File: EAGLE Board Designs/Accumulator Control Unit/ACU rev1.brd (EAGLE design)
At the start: 186.7 x 135.7 mm, 187 parts, among them J1 CONNECTOR-CAN_MF_T_V_, J2 CONNECTOR-8_MF_T_V_, J3 CONNECTOR-8_MF_T_V_, J4 CONNECTOR-2_MF_T_V_, J5 CONNECTOR-12_MF_T_V_, Q1 TRANSISTOR_N_MOS__PMV15ENEA, Q2 TRANSISTOR_N_MOS__PMV15ENEA, T1 TRANSFORMER_HM2112ZNLT_AIRGAP, U10 OPAMP_1_CHANNEL_OPA991, U11 LOGICGATE_AND_DCK3, U12 OPAMP_1_CHANNEL_OPA991, U13 OPAMP_1_CHANNEL_OPA991, U14 OPAMP_1_CHANNEL_OPA991, U15 LOGICGATE_AND_DCK3, U18 OPAMP_1_CHANNEL_OPA991, U19 MAX7404, U2 ADG1423, U20 OPAMP_1_CHANNEL_OPA991, U22 OPAMP_1_CHANNEL_OPA991, U25 TCAN1051HQV-Q1, U26 MAX7404, U27 OPAMP_1_CHANNEL_OPA991, U28 MAX7404, U29 OPAMP_1_CHANNEL_OPA991, U3 LM555, U30 MAX7404, U4 OPAMP_1_CHANNEL_OPA991, U5 LTC6820, U6 ADM823, U7 OPAMP_1_CHANNEL_OPA991, U8 LOGICGATE_AND_DCK3, U9 OPAMP_1_CHANNEL_OPA991

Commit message: minor via changes
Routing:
- net GND: track 187.6 -> 189.1 mm
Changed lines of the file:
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@@
 <drawing>
 <settings>
-<setting alwaysvectorfont="yes"/>
+<setting alwaysvectorfont="no"/>
 <setting verticaltext="up"/>
 </settings>
@@
 <wire x1="29.90349375" y1="59.00191875" x2="29.91529375" y2="59.01371875" width="0.1524" layer="1"/>
 <via x="29.91529375" y="59.01371875" extent="1-16" drill="0.3048" diameter="0.55"/>
-<wire x1="28.42939375" y1="58.04851875" x2="28.42939375" y2="59.28041875" width="0.1524" layer="1"/>
-<wire x1="28.42939375" y1="59.28041875" x2="28.46749375" y2="59.31851875" width="0.1524" layer="1"/>
-<via x="28.46749375" y="59.31851875" extent="1-16" drill="0.3048" diameter="0.55"/>
+<wire x1="28.42939375" y1="58.04851875" x2="28.42939375" y2="58.69621875" width="0.1524" layer="1"/>
+<wire x1="29.66129375" y1="59.92811875" x2="29.99149375" y2="59.92811875" width="0.1524" layer="1"/>
+<wire x1="29.66129375" y1="59.92811875" x2="28.42939375" y2="58.69621875" width="0.1524" layer="1"/>
+<via x="29.99149375" y="59.92811875" extent="1-16" drill="0.3048" diameter="0.55"/>
 <wire x1="169.43749375" y1="60.42251875" x2="169.43749375" y2="61.60451875" width="0.1524" layer="1"/>
 <via x="169.43749375" y="61.60451875" extent="1-16" drill="0.3048" diameter="0.55"/>
@@
 <wire x1="91.542225" y1="94.3795875" x2="88.555890625" y2="97.365921875" width="0.1524" layer="1"/>
 <wire x1="91.542225" y1="94.3795875" x2="91.439925" y2="94.3795875" width="0.1524" layer="1"/>
-<via x="29.259825" y="72.77214375" extent="1-16" drill="0.3048"/>
-<wire x1="28.64529375" y1="10.55051875" x2="28.64529375" y2="58.5982875" width="0.1524" layer="16"/>
-<wire x1="28.64529375" y1="58.5982875" x2="29.259825" y2="59.21281875" width="0.1524" layer="16"/>
-<wire x1="29.259825" y1="59.21281875" x2="29.259825" y2="72.77214375" width="0.1524" layer="16"/>
-<wire x1="53.316396875" y1="97.365921875" x2="29.259825" y2="73.30935" width="0.1524" layer="1"/>
-<wire x1="29.259825" y1="72.77214375" x2="29.259825" y2="73.30935" width="0.1524" layer="1"/>
+<via x="28.650225" y="70.63854375" extent="1-16" drill="0.3048"/>
+<wire x1="28.64529375" y1="70.6336125" x2="28.650225" y2="70.63854375" width="0.1524" layer="16"/>
+<wire x1="28.64529375" y1="70.6336125" x2="28.64529375" y2="10.55051875" width="0.1524" layer="16"/>
+<wire x1="53.316396875" y1="97.365921875" x2="28.650225" y2="72.69975" width="0.1524" layer="1"/>
+<wire x1="28.650225" y1="70.63854375" x2="28.650225" y2="72.69975" width="0.1524" layer="1"/>
 <wire x1="53.316396875" y1="97.365921875" x2="88.555890625" y2="97.365921875" width="0.1524" layer="1"/>
 <contactref element="IMD_OK_TEST" pad="1"/>
@@
 <wire x1="19.2275875" y1="6.52461875" x2="23.1645875" y2="6.52461875" width="0.1524" layer="16"/>
 <wire x1="23.1645875" y1="6.52461875" x2="25.2219875" y2="8.58201875" width="0.1524" layer="16"/>
-<via x="28.3255125" y="71.895478125" extent="1-16" drill="0.3048"/>
-<wire x1="28.3255125" y1="60.07456875" x2="28.3255125" y2="71.895478125" width="0.1524" layer="16"/>
-<wire x1="27.61659375" y1="10.38620625" x2="27.61659375" y2="59.36565" width="0.1524" layer="16"/>
-<wire x1="27.61659375" y1="59.36565" x2="28.3255125" y2="60.07456875" width="0.1524" layer="16"/>
-<wire x1="53.15028125" y1="97.69791875" x2="28.3255125" y2="72.87315" width="0.1524" layer="1"/>
-<wire x1="28.3255125" y1="71.895478125" x2="28.3255125" y2="72.87315" width="0.1524" layer="1"/>
+<via x="27.6397125" y="71.666878125" extent="1-16" drill="0.3048"/>
+<wire x1="27.61659375" y1="71.643759375" x2="27.6397125" y2="71.666878125" width="0.1524" layer="16"/>
+<wire x1="27.61659375" y1="71.643759375" x2="27.61659375" y2="10.38620625" width="0.1524" layer="16"/>
+<wire x1="53.15028125" y1="97.69791875" x2="27.6397125" y2="72.18735" width="0.1524" layer="1"/>
+<wire x1="27.6397125" y1="71.666878125" x2="27.6397125" y2="72.18735" width="0.1524" layer="1"/>
 <wire x1="100.67535" y1="92.37193125" x2="100.67535" y2="83.51155625" width="0.1524" layer="1"/>
 <wire x1="100.67535" y1="83.51155625" x2="96.553096875" y2="79.389303125" width="0.1524" layer="1"/>
@@
 <wire x1="15.89179375" y1="27.5059875" x2="16.32629375" y2="27.9404875" width="0.1524" layer="16"/>
 <wire x1="16.32629375" y1="27.9404875" x2="16.32629375" y2="57.79451875" width="0.1524" layer="16"/>
-<wire x1="22.42229375" y1="63.89051875" x2="23.69229375" y2="63.89051875" width="0.1524" layer="16"/>
-<via x="23.69229375" y="63.89051875" extent="1-16" drill="0.3048"/>
-<wire x1="16.32629375" y1="57.79451875" x2="22.42229375" y2="63.89051875" width="0.1524" layer="16"/>
+<wire x1="23.46369375" y1="64.93191875" x2="23.46369375" y2="64.95731875" width="0.1524" layer="16"/>
+<via x="23.46369375" y="64.95731875" extent="1-16" drill="0.3048"/>
+<wire x1="16.32629375" y1="57.79451875" x2="23.46369375" y2="64.93191875" width="0.1524" layer="16"/>
 <wire x1="177.70619375" y1="64.98271875" x2="184.74199375" y2="57.94691875" width="0.1524" layer="1"/>
 <wire x1="184.74199375" y1="57.94691875" x2="184.74199375" y2="51.99161875" width="0.1524" layer="1"/>
 <wire x1="184.74199375" y1="51.99161875" x2="183.63609375" y2="50.88571875" width="0.1524" layer="1"/>
-<wire x1="23.69229375" y1="63.89051875" x2="24.78449375" y2="64.98271875" width="0.1524" layer="1"/>
-<wire x1="177.70619375" y1="64.98271875" x2="24.78449375" y2="64.98271875" width="0.1524" layer="1"/>
+<wire x1="23.46369375" y1="64.95731875" x2="23.48909375" y2="64.98271875" width="0.1524" layer="1"/>
+<wire x1="177.70619375" y1="64.98271875" x2="23.48909375" y2="64.98271875" width="0.1524" layer="1"/>
 <wire x1="183.63609375" y1="50.88571875" x2="183.41529375" y2="50.87071875" width="0" layer="19" extent="1-1"/>
 </signal>

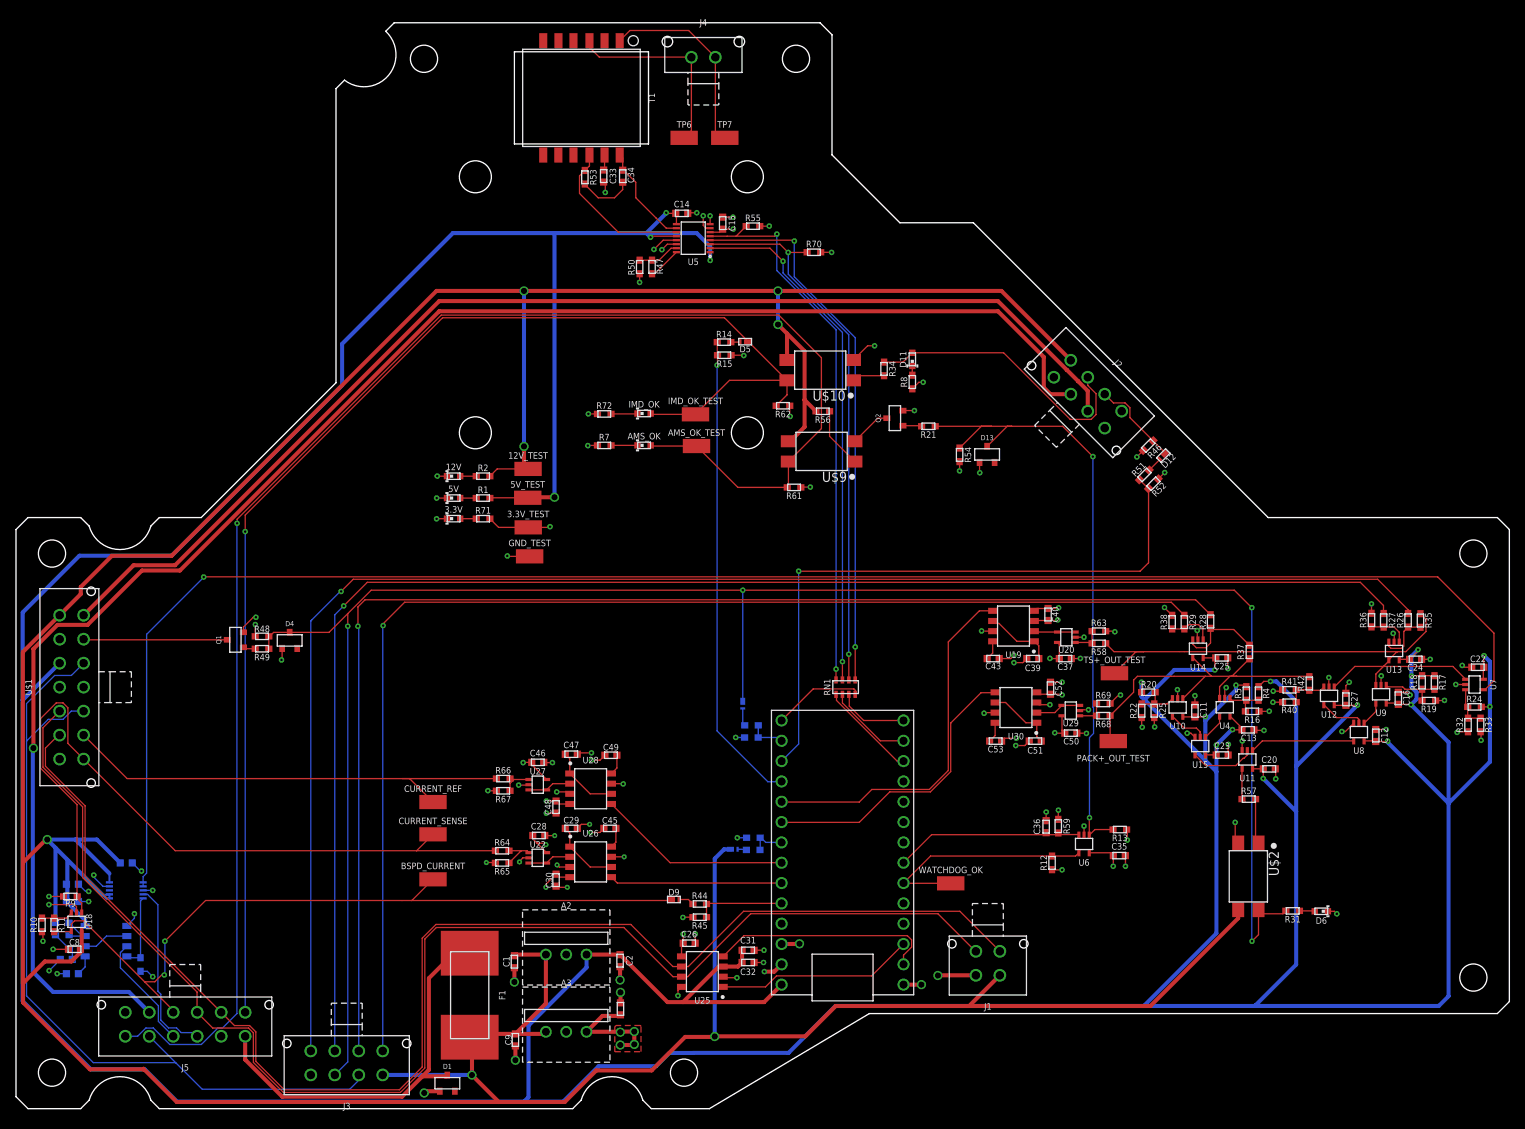
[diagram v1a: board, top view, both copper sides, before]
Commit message: Corrections
Added isolation barrier line
moved LTC6820 near teensy
moved precharger near connector
shdn traces now 20 mil
removed unneeded vias near 3.3V reg
mvoed caps of vregs inside keepouts
added 0603 LEDs for TSAL
mapped can tx and rx to D3 and D4 for compatibility with Teensy 3.2
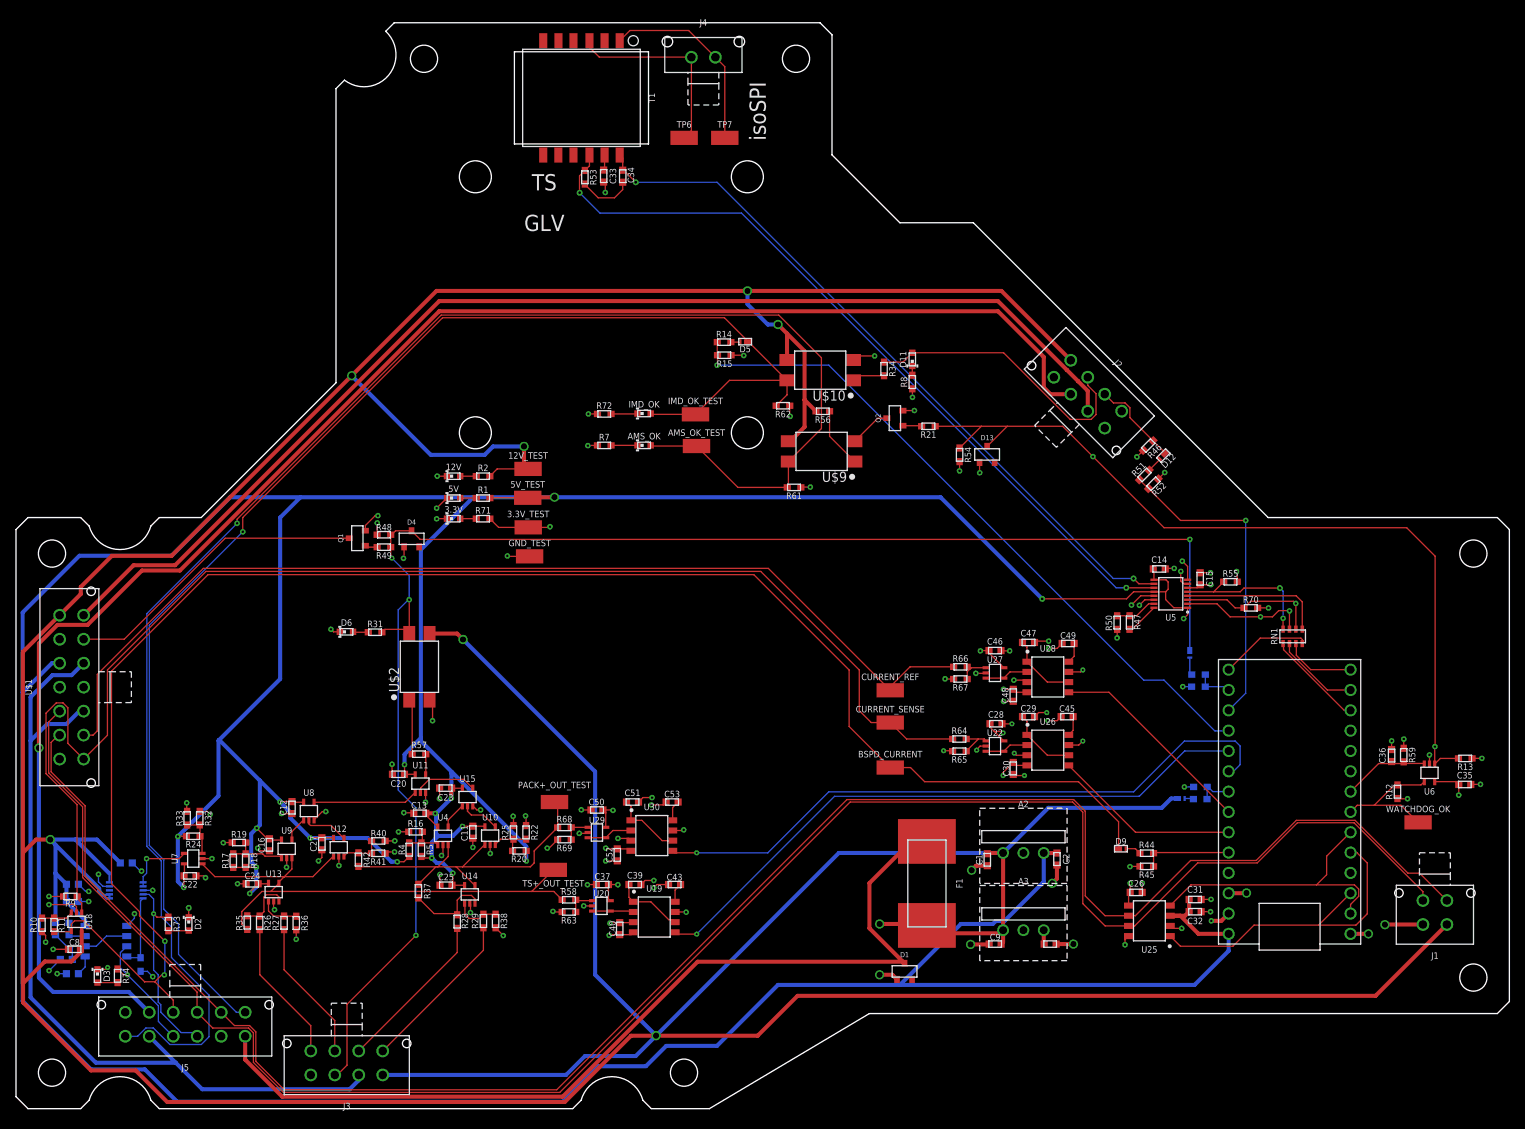
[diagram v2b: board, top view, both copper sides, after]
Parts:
- added D2: LED_0603_GREEN, HyTechDevices:0603-LED
- added D3: LED_0603_RED, HyTechDevices:0603-LED
- added R73, R74: RESISTOR_0603_2K, HyTechDevices:0603-RES
- added U$3: (no value), HyTechAesthetics:TS
- added U$4: (no value), HyTechAesthetics:ISOSPI
- added U$5: (no value), HyTechAesthetics:GLV
- moved C22 163.1 mm to (21.7, 27.6), turned to 0 degrees
- moved R33 162.1 mm to (21.4, 34.8), turned to 270 degrees
- moved U7 161.6 mm to (22.2, 29.8), turned to 90 degrees
- moved R24 161.0 mm to (22.2, 32.6), turned to 180 degrees
- moved R32 159.0 mm to (23.0, 34.8), turned to 270 degrees
- moved R17 151.8 mm to (27.2, 29.5), turned to 270 degrees
- moved R35 151.4 mm to (28.9, 21.8), turned to 270 degrees
- moved R19 149.8 mm to (27.9, 31.8), turned to 0 degrees
- moved R18 148.7 mm to (28.7, 29.5), turned to 270 degrees
- moved R26 148.4 mm to (30.5, 21.7), turned to 90 degrees
- moved C24 148.1 mm to (29.5, 26.6), turned to 180 degrees
- moved U13 143.3 mm to (32.2, 25.6), turned to 0 degrees
- moved R27 142.6 mm to (33.5, 21.7), turned to 90 degrees
- moved C16 142.3 mm to (31.7, 31.5), turned to 270 degrees
- moved R36 139.6 mm to (35.0, 21.7), turned to 270 degrees
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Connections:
- new net N$29: A1.D1, A1.D3, U25.1
- new net N$46: D3.2, R74.2
- net GND: now also D2.1, D3.1
- net N$24: now also D2.2, R73.2; no longer A1.D1, U25.1
- net N$25: now also A1.D4
- net TEENSY_OK: now also A1.D6; no longer A1.D5
- net TSAL_GREEN: now also R73.1
- net TSAL_RED: now also R74.1
- net WATCHDOG_INPUT: now also A1.D5; no longer A1.D4
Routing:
- net 60V_THRESHOLD: track 213.5 -> 8.64 mm
- net ISO_TS-: track 195.1 -> 17.8 mm, vias 1 -> 0
- net ISO_TS+: track 189.5 -> 17.8 mm, vias 1 -> 0
- net +12V: track 560.6 -> 723.4 mm, vias 7 -> 8
- net ISO_PACK-: track 163.3 -> 20.4 mm, vias 1 -> 0
- net ISO_PACK+: track 155.4 -> 20.6 mm, vias 1 -> 0
- net BSPD_CURRENT: track 97.2 -> 215.0 mm
- net N$35: track 19.4 -> 97.5 mm, vias 0 -> 2
- net N$38: track 12.9 -> 89.9 mm, vias 0 -> 2
- net CURRENT: track 97.3 -> 172.4 mm
- net +5V: track 720.5 -> 649.7 mm, vias 19 -> 18
- net CURRENT_REF: track 58.9 -> 129.3 mm
- net CANH: track 175.9 -> 243.6 mm
- net 12VIN: track 48.3 -> 115.2 mm
- net CANL: track 173.2 -> 239.7 mm
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- removed copper zone on layer 1, net +3V3

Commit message: adjust teensy position
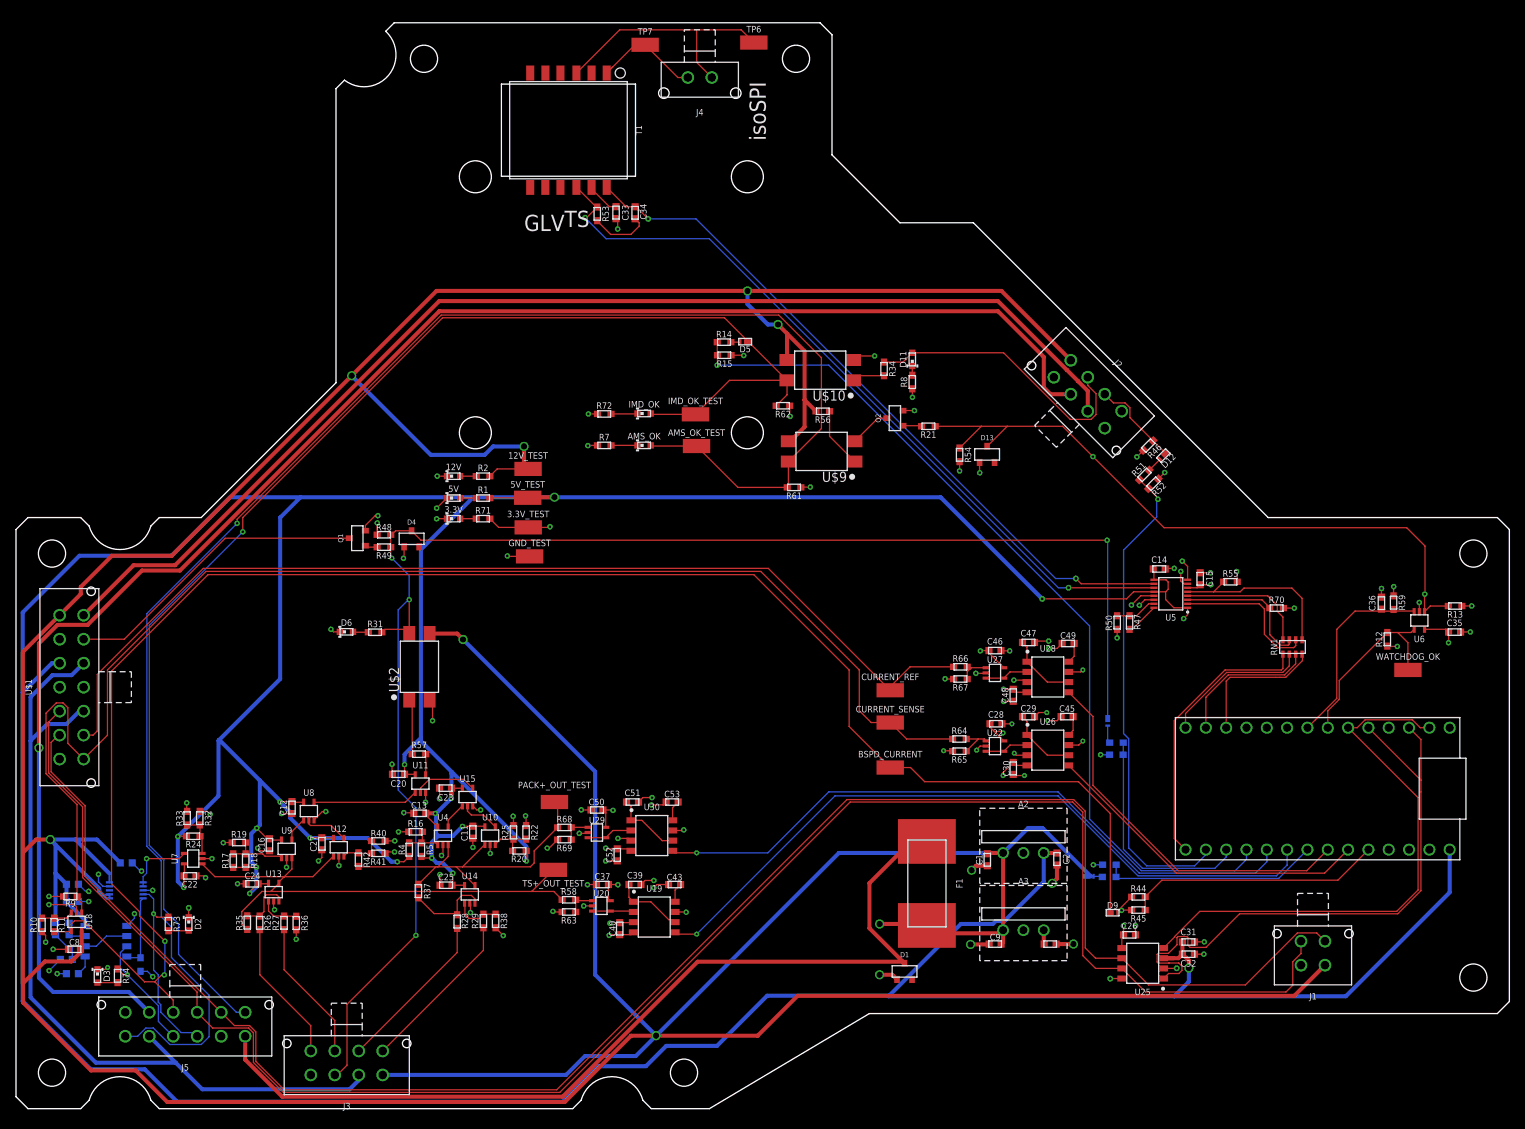
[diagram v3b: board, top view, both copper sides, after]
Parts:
- RN1: device HyTechDevices:1206-RES-ARRAY -> HyTechDevices - Copy:1206-RES-ARRAY
- moved A1 29.6 mm to (179.2, 30.9), turned to 90 degrees
- moved R12 19.1 mm to (171.4, 57.2)
- moved C36 19.1 mm to (170.7, 61.7)
- moved R13 19.1 mm to (179.9, 61.3)
- moved R59 19.1 mm to (172.2, 61.8)
- moved WATCHDOG_OK 19.1 mm to (174.0, 53.3)
- moved U6 19.1 mm to (175.4, 59.5)
- moved C35 19.1 mm to (179.8, 58.1)
- moved J1 16.1 mm to (162.1, 19.4)
- moved TP7 15.3 mm to (78.6, 131.5)
- moved R43 15.0 mm to (136.7, 29.0)
- moved D8 15.0 mm to (134.1, 27.5)
- moved R39 15.0 mm to (136.6, 27.5)
- moved TP6 14.8 mm to (92.2, 131.8)
- moved R23 13.3 mm to (137.6, 44.3)
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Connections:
- net CS_LTC_6820: now also RN1.5; no longer RN1.8
- net MHS_TEENSY: now also A1.D14; no longer A1.D15
- net N$13: now also RN1.8; no longer RN1.5
- net N$15: now also RN1.7; no longer RN1.6
- net N$18: now also RN1.6; no longer RN1.7
- net N$19: now also RN1.4; no longer RN1.1
- net N$21: now also RN1.3; no longer RN1.2
- net N$43: now also RN1.2; no longer RN1.3
- net N$44: now also RN1.1; no longer RN1.4
- net PACK+_FILTERED: now also A1.D17; no longer A1.D18
- net PRECHARGE_OK_TEENSY: now also A1.D15; no longer A1.D14
- net TS+_OUT_FILTERED: now also A1.D18; no longer A1.D17
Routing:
- net +5V: track 649.7 -> 685.1 mm, vias 18 -> 19
- net N$29: track 41.5 -> 76.3 mm
- net N$25: track 36.7 -> 69.7 mm
- net +12V: track 723.4 -> 696.7 mm
- net IMD_OK_TEENSY: track 85.8 -> 111.2 mm
- net PRECHARGE_OK_TEENSY: track 4.63 -> 28.7 mm
- net N$44: track 11.4 -> 34.8 mm
- net 12V_SCALED_3.3V: track 4.46 -> 27.2 mm
- net CURRENT_REF_FILTERED: track 26.2 -> 47.8 mm
- net BSPD_CURRENT_TEENSY: track 11.1 -> 32.1 mm
- net MHS_TEENSY: track 40.0 -> 60.8 mm
- net AMS_OK_3.3V: track 105.9 -> 86.3 mm
- net CURRENT_FILTERED: track 23.5 -> 41.7 mm
- net CANL: track 239.7 -> 225.9 mm
- net TEENSY_OK: track 11.2 -> 25.0 mm
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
